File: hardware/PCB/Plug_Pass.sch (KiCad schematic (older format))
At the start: 4 parts

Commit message: Upload KiCAD files
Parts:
- removed A?: Arduino_Nano_v3.x, Module:Arduino_Nano, symbol MCU_Module:Arduino_Nano_v3.x
- removed PS?: IRM-15-05, Converter_ACDC:Converter_ACDC_MeanWell_IRM-05-xx_THT, symbol Converter_ACDC:IRM-05-15
- removed RLY?: G5LE-14_DC5, digikey-footprints:Relay_THT_G5LE-14, symbol dk_Power-Relays-Over-2-Amps:G5LE-14_DC5
- removed U?: DS3231M, Package_SO:SOIC-16W_7.5x10.3mm_P1.27mm, symbol Timer_RTC:DS3231M
- added J?: Conn_WallSocket_Earth, symbol Plug_Pass:Conn_WallSocket_Earth
- added P1: Digital, Socket_Arduino_Nano:Socket_Strip_Arduino_1x15, symbol Connector_Generic:Conn_01x15
- added P2: Analog, Socket_Arduino_Nano:Socket_Strip_Arduino_1x15, symbol Connector_Generic:Conn_01x15
- added P3, P4, P5, P6: CONN_01X01, Socket_Arduino_Nano:1pin_Nano, symbol Connector_Generic:Conn_01x01
- added P?: Conn_WallPlug_Earth, symbol Plug_Pass:Conn_WallPlug_Earth
- added PS?: IRM-10-5, Converter_ACDC:Converter_ACDC_MeanWell_IRM-10-xx_THT, symbol Plug_Pass:IRM-10-5
- added RLY?: G5LE-14_DC5, digikey-footprints:Relay_THT_G5LE-14, symbol Plug_Pass:G5LE-14_DC5
- added U?: RF_PN532_Breakout, RF_Module:nRF24L01_Breakout, symbol Plug_Pass:RF_PN532_Breakout
- added U?: DS3231M, Package_SO:SOIC-16W_7.5x10.3mm_P1.27mm, symbol Plug_Pass:DS3231M
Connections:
- net labels added: +3.3V, +5V, 0(Rx), 1(Tx), 10(**/SS), 11(**/MOSI), 12(MISO), 13(SCK), 2, 3(**), 4, 5(**), 6(**), 7, 8, 9(**), A0, A1, A2, A3, A4, A5, A6, A7, AREF, GND, GNDREF, Reset, VCC, Vin
- wire segments 0 -> 72
- no-connect marks 0 -> 4
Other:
- note added: "1"
- note added: "Holes"
- note added: "Shield for Arduino Nano"

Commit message: add current files through upload
includes revised schematic and updated library with parts
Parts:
- removed J?: Conn_WallSocket_Earth, symbol Plug_Pass:Conn_WallSocket_Earth
- removed P3, P4, P5, P6: CONN_01X01, Socket_Arduino_Nano:1pin_Nano, symbol Connector_Generic:Conn_01x01
- removed P?: Conn_WallPlug_Earth, symbol Plug_Pass:Conn_WallPlug_Earth
- added J? (x6): Conn_01x15_MountingPin, symbol Plug_Pass:Conn_01x15_MountingPin
- added J? (x2): Conn_01x08, symbol Plug_Pass:Conn_01x08
- added J? (x2): Conn_01x06, symbol Plug_Pass:Conn_01x06
- added J?: OSTTC030162, digikey-footprints:Term_Block_1x3_P5mm, symbol Plug_Pass:OSTTC030162
- added J?: Conn_WallSocket_Earth, symbol Plug_Pass:Conn_WallSocket_Earth
- added U? (x2): QuickDisconnect, symbol Plug_Pass:QuickDisconnect
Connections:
- net labels added: +3V3, 32K, 5V, D0(Rx), D1(Tx), D10, D11, D12, D13, D2, D3, D4, D5, D6, D7, D8, D9, IRQ, LINE, MISO, MOSI, NEUT, RSTO, SCK, SCL, SDA, SQW, SS, VIN
- net labels removed: +3.3V, 0(Rx), 1(Tx), 10(**/SS), 11(**/MOSI), 12(MISO), 13(SCK), 2, 3(**), 4, 5(**), 6(**), 7, 8, 9(**)
- wire segments 72 -> 140
- no-connect marks 4 -> 53
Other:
- note added: "NFC RFID PN532 Module"
- note added: "Real-Time Clock Module - DS3231 AT24C32"
- note added: "Shield for breakout modules"
- note removed: "Holes"
- moved on the sheet: PS?, RLY?

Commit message: Schematic update for SPI wiring of NFC reader
Corresponding update to the PCB schematic to correspond to the firmware update.
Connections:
- wire segments 140 -> 141
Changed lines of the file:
@@
 Text Label 9000 2700 2    50   ~ 0
 GND
-Wire Wire Line
-	8000 1850 8250 1850
-Wire Wire Line
-	8250 1850 8250 2200
-Wire Wire Line
-	8250 2200 9000 2200
-Wire Wire Line
-	8000 1950 8350 1950
-Wire Wire Line
-	8350 1950 8350 2400
-Wire Wire Line
-	8350 2400 9000 2400
-Wire Wire Line
-	8000 2050 8450 2050
-Wire Wire Line
-	8450 2050 8450 2500
-Wire Wire Line
-	8450 2500 9000 2500
-Wire Wire Line
-	8000 2150 8550 2150
-Wire Wire Line
-	8550 2150 8550 2300
-Wire Wire Line
-	8550 2300 9000 2300
 Text Label 9000 2500 2    50   ~ 0
 SS
@@
 	4950 7400 4950 6800
 Wire Wire Line
-	4950 6800 5600 6800
+	4950 6800 5500 6800
 Text Label 1650 5850 0    50   ~ 0
 D12
@@
 NoConn ~ 8000 1450
 NoConn ~ 4150 5000
+$Comp
+L power:LINE #PWR?
+U 1 1 5E94FB8A
+P 5500 6800
+F 0 "#PWR?" H 5500 6650 50  0001 C CNN
+F 1 "LINE" H 5350 6850 50  0000 C CNN
+F 2 "" H 5500 6800 50  0001 C CNN
+F 3 "" H 5500 6800 50  0001 C CNN
+	1    5500 6800
+	1    0    0    -1
+$EndComp
+Connection ~ 5500 6800
+Wire Wire Line
+	5500 6800 5600 6800
+Wire Wire Line
+	8600 1850 8600 2200
+Wire Wire Line
+	8600 2200 9000 2200
+Wire Wire Line
+	8000 1850 8600 1850
+Wire Wire Line
+	8000 1950 8500 1950
+Wire Wire Line
+	8500 1950 8500 2300
+Wire Wire Line
+	8500 2300 9000 2300
+Wire Wire Line
+	8000 2050 8400 2050
+Wire Wire Line
+	8400 2050 8400 2400
+Wire Wire Line
+	8400 2400 9000 2400
+Wire Wire Line
+	8000 2150 8300 2150
+Wire Wire Line
+	8300 2150 8300 2500
+Wire Wire Line
+	8300 2500 9000 2500
 $EndSCHEMATC

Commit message: Uploaded revised schematic and pcb layout
Uploaded revisions to the KiCAD schematic, and included phase 1 of the PCB layout design process.
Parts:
- removed J? (x6): Conn_01x15_MountingPin, symbol Plug_Pass:Conn_01x15_MountingPin
- removed J?: Conn_01x08, symbol Plug_Pass:Conn_01x08
- removed J?: Conn_01x06, symbol Plug_Pass:Conn_01x06
- removed J?: OSTTC030162, digikey-footprints:Term_Block_1x3_P5mm, symbol Plug_Pass:OSTTC030162
- removed P1: Digital, Socket_Arduino_Nano:Socket_Strip_Arduino_1x15, symbol Connector_Generic:Conn_01x15
- removed P2: Analog, Socket_Arduino_Nano:Socket_Strip_Arduino_1x15, symbol Connector_Generic:Conn_01x15
- removed U?: RF_PN532_Breakout, RF_Module:nRF24L01_Breakout, symbol Plug_Pass:RF_PN532_Breakout
- removed U?: DS3231M, Package_SO:SOIC-16W_7.5x10.3mm_P1.27mm, symbol Plug_Pass:DS3231M
- added A1: Arduino_Nano_v3.x, Plug_Pass:Arduino_Nano_WithMountingHoles, symbol Plug_Pass:Arduino_Nano_v3.x
- added J10: TDPT-1017503, Plug_Pass:TDPT_2P_5.08MM, symbol Plug_Pass:TDPT-1017503
- added J3: Conn_01x06, Plug_Pass:PinHeader_1x06_P2.54mm_Vertical, symbol Plug_Pass:Conn_01x06
- added J4, J6: QuickDisconnect, symbol Plug_Pass:QuickDisconnect
- added J7: Conn_01x06, Plug_Pass:PinSocket_1x06_P2.54mm_Vertical, symbol Plug_Pass:Conn_01x06
- added RLY2: T95S5D22-5, Plug_Pass:RLY-T9AS5D22-5, symbol Plug_Pass:G5LE-14_DC5
- J1: renamed from J?; footprint (none) -> Plug_Pass:PinSocket_1x06_P2.54mm_Vertical
- J2: renamed from J?; footprint (none) -> Plug_Pass:PinSocket_1x08_P2.54mm_Vertical
- PS1: renamed from PS?; value IRM-10-5 -> IRM-15-5; footprint Converter_ACDC:Converter_ACDC_MeanWell_IRM-10-xx_THT -> Plug_Pass:Converter_ACDC_MeanWell_IRM-15-5_THT; Digi-Key Part Number (none) -> 1866-3037-ND
- RLY1: renamed from RLY?; value G5LE-14_DC5 -> T95S5D22-5; footprint digikey-footprints:Relay_THT_G5LE-14 -> Plug_Pass:RLY-T9AS5D22-5; DK_Datasheet_Link https://omronfs.omron.com/en_US/ecb/products/pdf/en-g5le.pdf -> https://www.te.com/commerce/DocumentDelivery/DDEController?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; DK_Detail_Page /product-detail/en/omron-electronics-inc-emc-div/G5LE-14-DC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 -> https://www.digikey.com/product-detail/en/te-connectivity-p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; Description RELAY GEN PURPOSE SPDT 10A 5V -> RELAY GEN PURPOSE SPDT 20A 5V; Digi-Key_PN Z1011-ND -> PB1015-ND; MPN G5LE-14 DC5 -> T9AS5D22-5; Manufacturer Omron Electronics Inc-EMC Div -> TE Connectivity Potter & Brumfield Relays
- gave numbers to parts that had none: 3
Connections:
- net labels added: RelayPin, VAC
- net labels removed: 5V, A0, A1, A2, A3, A4, A5, A6, A7, AREF, D0(Rx), D1(Tx), D10, D11, D12, D13, D2, D3, D4, D5, D6, D7, D8, D9, LINE, Reset, VIN, Vin
- wire segments 141 -> 68
- no-connect marks 53 -> 34
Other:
- note added: "Female header connector \nfor arduino shield attachment"
- note added: "Female socket connector \nfor PN532 NFC Module"
- note added: "Female socket connector \nfor RTC3231 module"
- note added: "Male header connector \nfor power supply and\nrelay shield"
- note added: "Open connection \nfor expansion \nto 240V outlet"
- note added: "Primary voltages to relay and outlets are hand\nwired, not printed on circuit board."
- note added: "Shield for Arduino Nano, PN532, and RTC3231 sockets"
- note added: "Shield for Power Supply and Relay shield"
- note removed: "1"
- note removed: "NFC RFID PN532 Module"
- note removed: "Real-Time Clock Module - DS3231 AT24C32"
- note removed: "Shield for Arduino Nano"
- note removed: "Shield for breakout modules"
- moved on the sheet: J1, J2, J5, J8, J9, PS1, RLY1

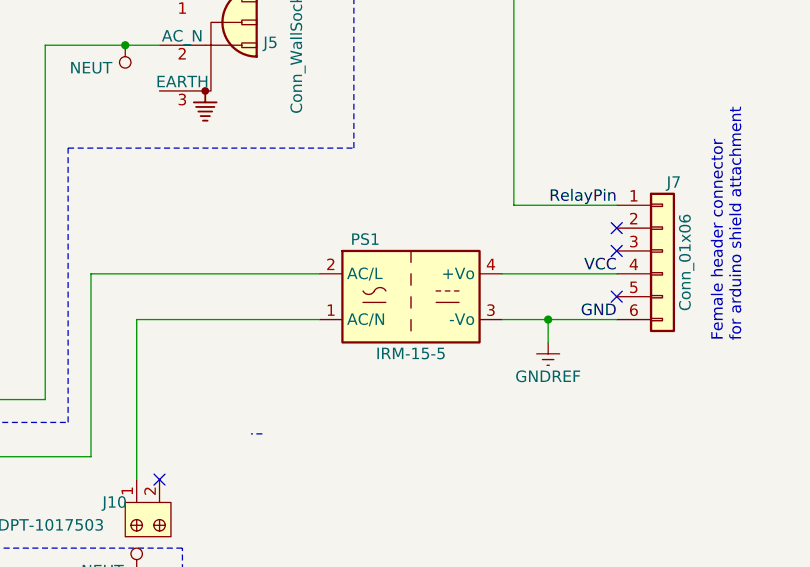
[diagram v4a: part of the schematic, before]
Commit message: Version 1 of a full PCB design
This push has a full KiCAD package for a set of boards.  Still in draft, but it's complete.
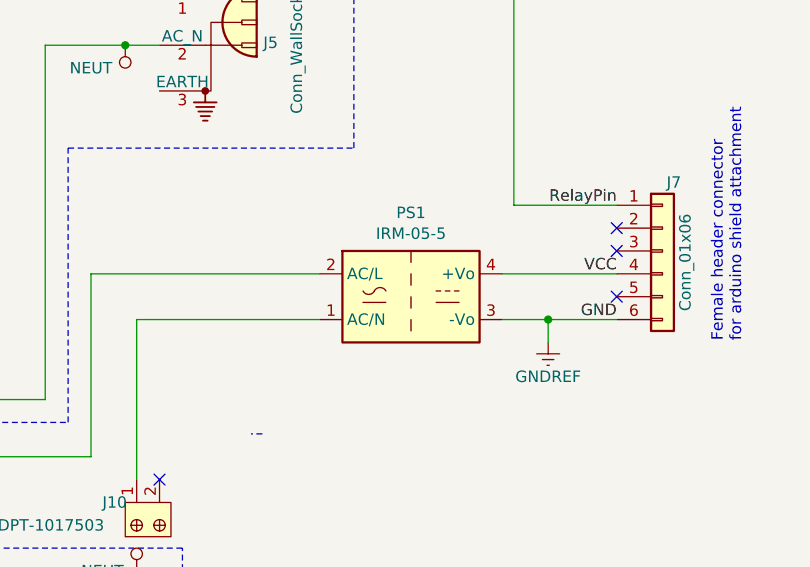
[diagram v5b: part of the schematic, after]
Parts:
- removed PS1: IRM-15-5, Plug_Pass:Converter_ACDC_MeanWell_IRM-15-5_THT, symbol Plug_Pass:IRM-10-5
- added PS1: IRM-05-5, Plug_Pass:Converter_ACDC_MeanWell_IRM-05-xx_THT, symbol Plug_Pass:IRM-05-5
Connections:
- net +5V: now also PS1.4 (+Vo)
- net GNDREF: now also PS1.3 (-Vo)
- net at J10.1: now also PS1.1 (AC/N)
- net at J9.~, RLY1.1 (COM): now also PS1.2 (AC/L)
- net at J4.~: now also RLY2.3 (NO)
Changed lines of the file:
@@
-$EndComp
-$Comp
-L Plug_Pass:IRM-10-5 PS1
-U 1 1 5E90266B
-P 7650 5950
-F 0 "PS1" H 7450 6200 50  0000 C CNN
-F 1 "IRM-15-5" H 7650 5700 50  0000 C CNN
-F 2 "Plug_Pass:Converter_ACDC_MeanWell_IRM-15-5_THT" H 7650 5600 50  0001 C CNN
-F 3 "https://www.meanwell.com/Upload/PDF/IRM-15/IRM-15-SPEC.PDF" H 7650 5550 50  0001 C CNN
-F 4 "1866-3037-ND" H 7650 5950 50  0001 C CNN "Digi-Key Part Number"
-	1    7650 5950
-	1    0    0    -1
 $EndComp
 $Comp
@@
 	1    0    0    -1
 $EndComp
+$Comp
+L Plug_Pass:IRM-05-5 PS1
+U 1 1 5E98A7A4
+P 7650 5950
+F 0 "PS1" H 7650 6317 50  0000 C CNN
+F 1 "IRM-05-5" H 7650 6226 50  0000 C CNN
+F 2 "Plug_Pass:Converter_ACDC_MeanWell_IRM-05-xx_THT" H 7650 5600 50  0001 C CNN
+F 3 "https://www.meanwell.com/Upload/PDF/IRM-05/IRM-05-SPEC.PDF" H 7650 5550 50  0001 C CNN
+	1    7650 5950
+	1    0    0    -1
+$EndComp

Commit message: Add files via upload
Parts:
- removed J3: Conn_01x06, Plug_Pass:PinHeader_1x06_P2.54mm_Vertical, symbol Plug_Pass:Conn_01x06
- removed J4, J6: QuickDisconnect, symbol Plug_Pass:QuickDisconnect
- removed J7: Conn_01x06, Plug_Pass:PinSocket_1x06_P2.54mm_Vertical, symbol Plug_Pass:Conn_01x06
- removed RLY2: T95S5D22-5, Plug_Pass:RLY-T9AS5D22-5, symbol Plug_Pass:G5LE-14_DC5
- added J3, J4: Conn_02x04_Odd_Even, Plug_Pass:IDC-Header_2x04_P2.54mm_Vertical, symbol Plug_Pass:Conn_02x04_Odd_Even
- added RLY2: G5V-1-DC5, Plug_Pass:Relay_THT_G5V-1, symbol Plug_Pass:G5V-1-DC5
- J10: footprint Plug_Pass:TDPT_2P_5.08MM -> Plug_Pass:TDPT_2P_6.35MM
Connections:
- net +5V: no longer A1.30 (VIN), PS1.4 (+Vo)
- net GNDREF: now also J10.2, J3.7 (Pin_7), J4.7 (Pin_7), RLY2.9 (COIL)
- net RelayPin: now also J3.1 (Pin_1), J4.1 (Pin_1), RLY2.10 (NO); no longer A1.15 (D12)
- net Earth: now reaches J5.3 (EARTH)
- new net: A1.15 (D12), RLY2.2 (COIL)
- new net VCC: A1.30 (VIN), J3.5 (Pin_5), J4.5 (Pin_5), PS1.4 (+Vo), RLY2.5 (COM), RLY2.6 (COM)
- no-connect marks 34 -> 36
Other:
- note added: "Ribbon connector for\npower supply and\nrelay shield"
- note removed: "Female header connector \nfor arduino shield attachment"
- note removed: "Male header connector \nfor power supply and\nrelay shield"

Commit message: Add files via upload
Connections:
- net RLY2-Pin: now reaches A1.15 (D12), RLY2.2 (COIL)
- net RLY2-Pin: now also J3.1 (Pin_1), J4.1 (Pin_1)
- net RelayPin renamed RLY1-Pin
- net RLY1-Pin: no longer J3.1 (Pin_1), J4.1 (Pin_1)
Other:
- note added: "AC Shield\nfor Power Supply and Relay shield"
- note added: "Arduino Shield\nfor Arduino Nano, PN532, and RTC3231 sockets"
- note removed: "Open connection \nfor expansion \nto 240V outlet"
- note removed: "Shield for Arduino Nano, PN532, and RTC3231 sockets"
- note removed: "Shield for Power Supply and Relay shield"
- moved on the sheet: J10, J3, J4, J8, J9, PS1, RLY1
